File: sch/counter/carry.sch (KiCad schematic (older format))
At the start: 9 parts, among them Q34 Q_NMOS_GSD, Q35 Q_NMOS_GSD

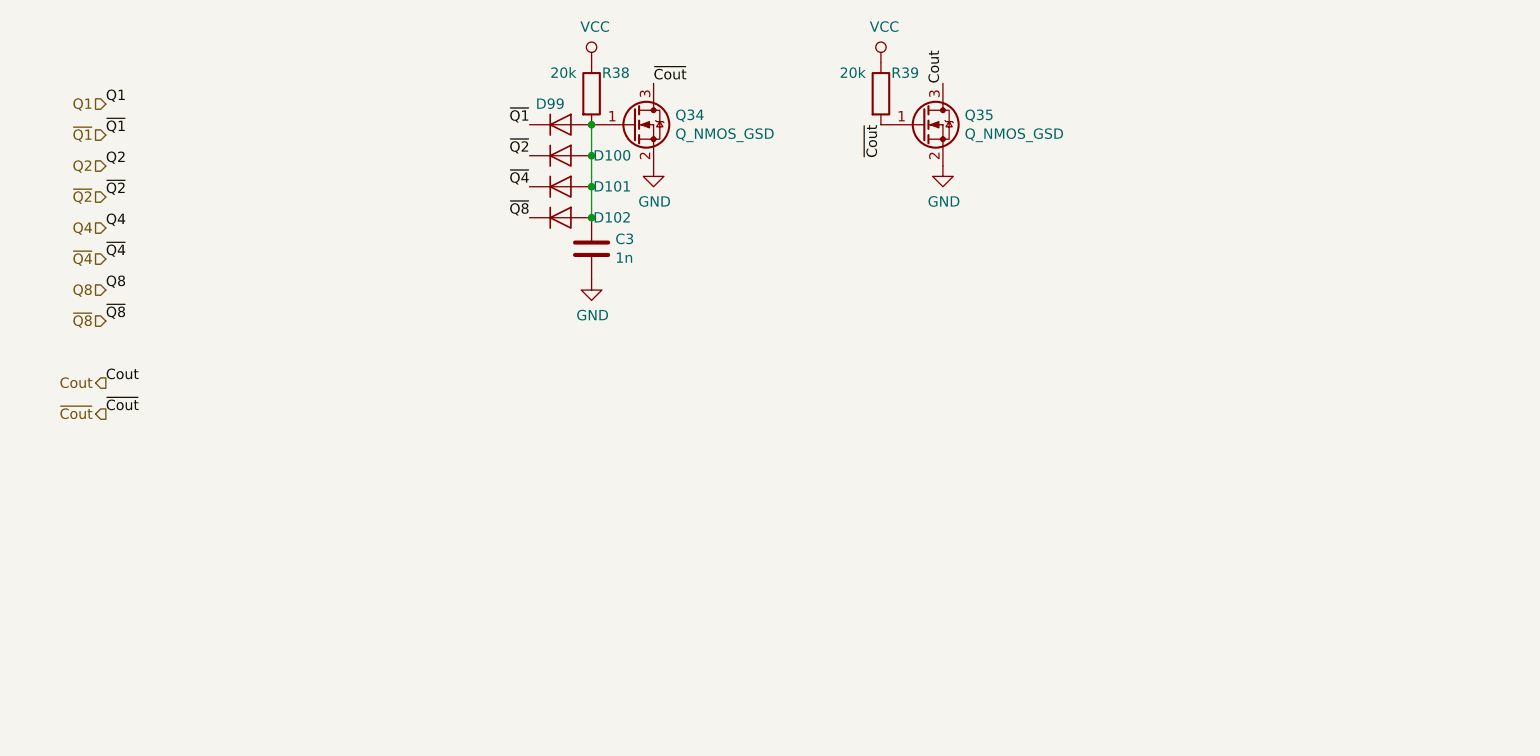
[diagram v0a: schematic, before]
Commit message: Counter schematic improvements
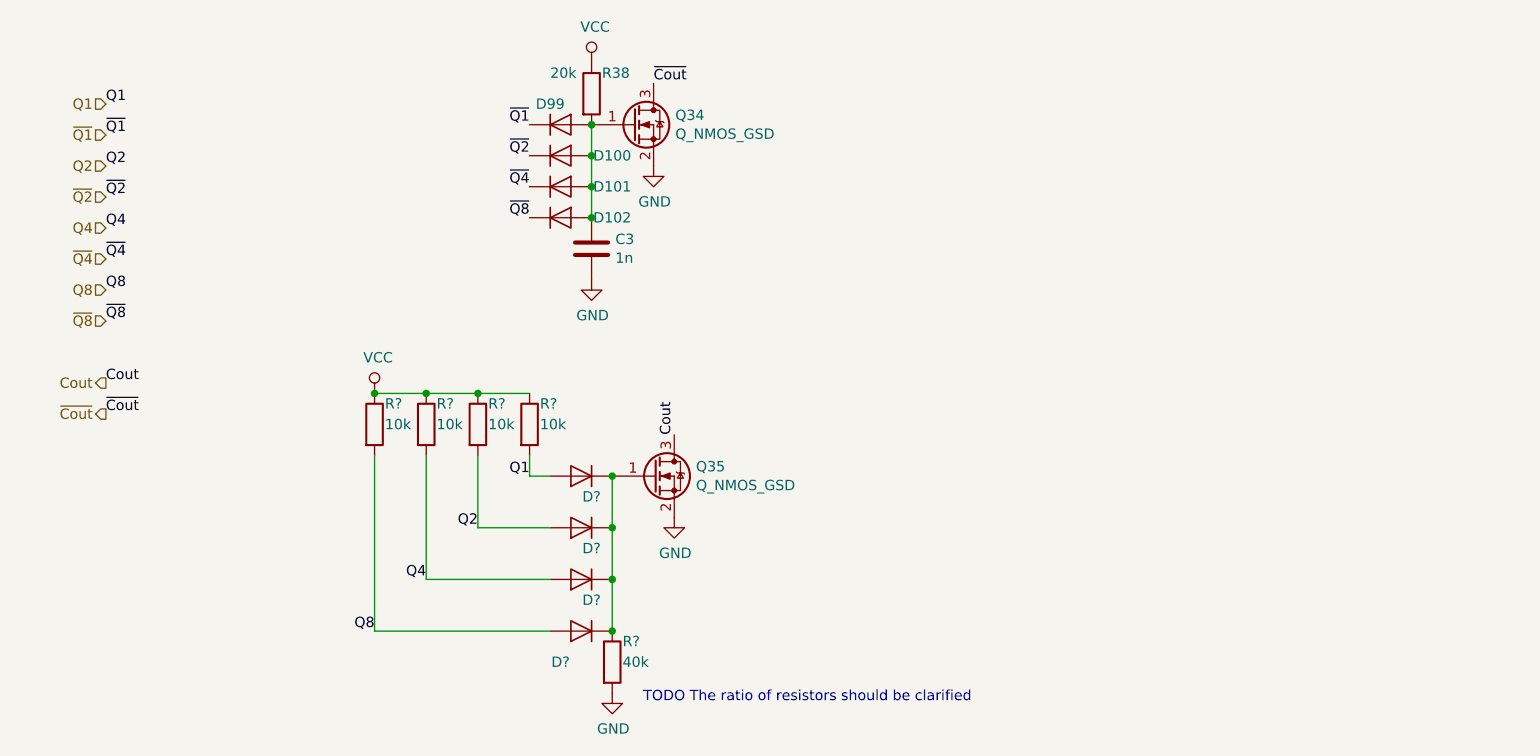
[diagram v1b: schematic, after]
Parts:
- removed R39: 20k, symbol Device:R
- added D? (x4): D, symbol Device:D
- added R? (x4): 10k, symbol Device:R
- added R?: 40k, symbol Device:R
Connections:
- net GND: now also R?.2
- net Q1: now also D?.2 (A), R?.2
- net Q2: now also D?.2 (A), R?.2
- net Q4: now also D?.2 (A), R?.2
- net Q8: now also D?.2 (A), R?.2
- net VCC: now also R?.1, R?.1, R?.1, R?.1
- net ~Cout: no longer Q35.1 (G)
- new net: D?.1 (K), D?.1 (K), D?.1 (K), D?.1 (K), Q35.1 (G), R?.1
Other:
- note added: "TODO The ratio of resistors should be clarified"
- moved on the sheet: Q35

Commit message: One flip-flop is placed on PCB
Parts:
- C3: footprint (none) -> Capacitor_SMD:C_0805_2012Metric
- D100, D101, D102, D99: footprint (none) -> Diode_SMD:D_MiniMELF
- D103, D104, D105, D106: renamed from D?; footprint (none) -> Diode_SMD:D_MiniMELF
- Q34, Q35: footprint (none) -> Package_TO_SOT_SMD:SOT-23
- R38, R39, R40, R41, R43: renamed from R?; footprint (none) -> Resistor_SMD:R_0805_2012Metric
- R42: renamed from R38; footprint (none) -> Resistor_SMD:R_0805_2012Metric
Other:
- note added: "This capacitor is needed to avoid driving ~Cout~ down too quickly.\nThis happens when the lower bits are reset and the higher bit is set (3->4, 1->2, etc.)."
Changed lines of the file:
@@
 EESchema Schematic File Version 4
+LIBS:counter-cache
 EELAYER 26 0
 EELAYER END
@@
 F 0 "Q34" H 4005 1196 50  0000 L CNN
 F 1 "Q_NMOS_GSD" H 4005 1105 50  0000 L CNN
-F 2 "" H 4000 1250 50  0001 C CNN
+F 2 "Package_TO_SOT_SMD:SOT-23" H 4000 1250 50  0001 C CNN
 F 3 "~" H 3800 1150 50  0001 C CNN
 	1    3800 1150
@@
 AR Path="/5BF4F50C/5BF5F56C" Ref="R?"  Part="1"
 AR Path="/5BF4F514/5BF5F56C" Ref="R?"  Part="1"
-AR Path="/5BF5F0A6/5BF5F56C" Ref="R38"  Part="1"
-F 0 "R38" H 3650 1100 50  0000 L CNN
+AR Path="/5BF5F0A6/5BF5F56C" Ref="R42"  Part="1"
+F 0 "R42" H 3650 1100 50  0000 L CNN
 F 1 "20k" H 3400 1100 50  0000 L CNN
-F 2 "" V 3530 1000 50  0001 C CNN
+F 2 "Resistor_SMD:R_0805_2012Metric" V 3530 1000 50  0001 C CNN
 F 3 "~" H 3600 1000 50  0001 C CNN
 	1    3600 1000
@@
 F 0 "D99" H 3400 1250 50  0000 C CNN
 F 1 "D" H 3450 1275 50  0001 C CNN
-F 2 "" H 3450 1150 50  0001 C CNN
+F 2 "Diode_SMD:D_MiniMELF" H 3450 1150 50  0001 C CNN
 F 3 "~" H 3450 1150 50  0001 C CNN
 	1    3450 1150
@@
 F 0 "D100" H 3700 1300 50  0000 C CNN
 F 1 "D" H 3450 1425 50  0001 C CNN
-F 2 "" H 3450 1300 50  0001 C CNN
+F 2 "Diode_SMD:D_MiniMELF" H 3450 1300 50  0001 C CNN
 F 3 "~" H 3450 1300 50  0001 C CNN
 	1    3450 1300
@@
 F 0 "D101" H 3700 1450 50  0000 C CNN
 F 1 "D" H 3200 1450 50  0001 C CNN
-F 2 "" H 3450 1450 50  0001 C CNN
+F 2 "Diode_SMD:D_MiniMELF" H 3450 1450 50  0001 C CNN
 F 3 "~" H 3450 1450 50  0001 C CNN
 	1    3450 1450
@@
 AR Path="/5BF4F50C/5BF5F58F" Ref="#PWR?"  Part="1"
 AR Path="/5BF4F514/5BF5F58F" Ref="#PWR?"  Part="1"
-AR Path="/5BF5F0A6/5BF5F58F" Ref="#PWR077"  Part="1"
-F 0 "#PWR077" H 3600 700 50  0001 C CNN
+AR Path="/5BF5F0A6/5BF5F58F" Ref="#PWR078"  Part="1"
+F 0 "#PWR078" H 3600 700 50  0001 C CNN
 F 1 "VCC" H 3617 1023 50  0000 C CNN
 F 2 "" H 3600 850 50  0001 C CNN
@@
 $EndComp
 $Comp
-L power:GND #PWR079
+L power:GND #PWR081
 U 1 1 5BF5F5F2
 P 3900 1350
-F 0 "#PWR079" H 3900 1100 50  0001 C CNN
+F 0 "#PWR081" H 3900 1100 50  0001 C CNN
 F 1 "GND" H 3905 1177 50  0000 C CNN
 F 2 "" H 3900 1350 50  0001 C CNN
@@
 F 0 "D102" H 3700 1600 50  0000 C CNN
 F 1 "D" H 3450 1725 50  0001 C CNN
-F 2 "" H 3450 1600 50  0001 C CNN
+F 2 "Diode_SMD:D_MiniMELF" H 3450 1600 50  0001 C CNN
 F 3 "~" H 3450 1600 50  0001 C CNN
 	1    3450 1600
@@
 F 0 "C3" H 3715 1796 50  0000 L CNN
 F 1 "1n" H 3715 1705 50  0000 L CNN
-F 2 "" H 3638 1600 50  0001 C CNN
+F 2 "Capacitor_SMD:C_0805_2012Metric" H 3638 1600 50  0001 C CNN
 F 3 "~" H 3600 1750 50  0001 C CNN
 	1    3600 1750
@@
 Connection ~ 3600 1600
 $Comp
-L power:GND #PWR078
+L power:GND #PWR079
 U 1 1 5BF5F81C
 P 3600 1900
-F 0 "#PWR078" H 3600 1650 50  0001 C CNN
+F 0 "#PWR079" H 3600 1650 50  0001 C CNN
 F 1 "GND" H 3605 1727 50  0000 C CNN
 F 2 "" H 3600 1900 50  0001 C CNN
@@
 F 0 "Q35" H 4105 2896 50  0000 L CNN
 F 1 "Q_NMOS_GSD" H 4105 2805 50  0000 L CNN
-F 2 "" H 4100 2950 50  0001 C CNN
+F 2 "Package_TO_SOT_SMD:SOT-23" H 4100 2950 50  0001 C CNN
 F 3 "~" H 3900 2850 50  0001 C CNN
 	1    3900 2850
@@
 $EndComp
 $Comp
-L power:GND #PWR081
+L power:GND #PWR082
 U 1 1 5BF5F8BF
 P 4000 3050
-F 0 "#PWR081" H 4000 2800 50  0001 C CNN
+F 0 "#PWR082" H 4000 2800 50  0001 C CNN
 F 1 "GND" H 4005 2877 50  0000 C CNN
 F 2 "" H 4000 3050 50  0001 C CNN
@@
 AR Path="/5BF4F50C/5BF92A86" Ref="D?"  Part="1"
 AR Path="/5BF4F514/5BF92A86" Ref="D?"  Part="1"
-AR Path="/5BF5F0A6/5BF92A86" Ref="D?"  Part="1"
-F 0 "D?" H 3500 2950 50  0000 C CNN
+AR Path="/5BF5F0A6/5BF92A86" Ref="D103"  Part="1"
+F 0 "D103" H 3500 2950 50  0000 C CNN
 F 1 "D" H 3550 2975 50  0001 C CNN
-F 2 "" H 3550 2850 50  0001 C CNN
+F 2 "Diode_SMD:D_MiniMELF" H 3550 2850 50  0001 C CNN
 F 3 "~" H 3550 2850 50  0001 C CNN
 	1    3550 2850
@@
 AR Path="/5BF4F50C/5BF92B23" Ref="D?"  Part="1"
 AR Path="/5BF4F514/5BF92B23" Ref="D?"  Part="1"
-AR Path="/5BF5F0A6/5BF92B23" Ref="D?"  Part="1"
-F 0 "D?" H 3500 3200 50  0000 C CNN
+AR Path="/5BF5F0A6/5BF92B23" Ref="D104"  Part="1"
+F 0 "D104" H 3500 3200 50  0000 C CNN
 F 1 "D" H 3550 3225 50  0001 C CNN
-F 2 "" H 3550 3100 50  0001 C CNN
+F 2 "Diode_SMD:D_MiniMELF" H 3550 3100 50  0001 C CNN
 F 3 "~" H 3550 3100 50  0001 C CNN
 	1    3550 3100
@@
 AR Path="/5BF4F50C/5BF92B48" Ref="D?"  Part="1"
 AR Path="/5BF4F514/5BF92B48" Ref="D?"  Part="1"
-AR Path="/5BF5F0A6/5BF92B48" Ref="D?"  Part="1"
-F 0 "D?" H 3500 3450 50  0000 C CNN
+AR Path="/5BF5F0A6/5BF92B48" Ref="D105"  Part="1"
+F 0 "D105" H 3500 3450 50  0000 C CNN
 F 1 "D" H 3550 3475 50  0001 C CNN
-F 2 "" H 3550 3350 50  0001 C CNN
+F 2 "Diode_SMD:D_MiniMELF" H 3550 3350 50  0001 C CNN
 F 3 "~" H 3550 3350 50  0001 C CNN
 	1    3550 3350
@@
 AR Path="/5BF4F50C/5BF92B6F" Ref="D?"  Part="1"
 AR Path="/5BF4F514/5BF92B6F" Ref="D?"  Part="1"
-AR Path="/5BF5F0A6/5BF92B6F" Ref="D?"  Part="1"
-F 0 "D?" H 3650 3750 50  0000 C CNN
+AR Path="/5BF5F0A6/5BF92B6F" Ref="D106"  Part="1"
+F 0 "D106" H 3650 3750 50  0000 C CNN
 F 1 "D" H 3550 3725 50  0001 C CNN
-F 2 "" H 3550 3600 50  0001 C CNN
+F 2 "Diode_SMD:D_MiniMELF" H 3550 3600 50  0001 C CNN
 F 3 "~" H 3550 3600 50  0001 C CNN
 	1    3550 3600
@@
 AR Path="/5BF4F50C/5BF92BB5" Ref="R?"  Part="1"
 AR Path="/5BF4F514/5BF92BB5" Ref="R?"  Part="1"
-AR Path="/5BF5F0A6/5BF92BB5" Ref="R?"  Part="1"
-F 0 "R?" H 3350 2700 50  0000 L CNN
+AR Path="/5BF5F0A6/5BF92BB5" Ref="R41"  Part="1"
+F 0 "R41" H 3350 2700 50  0000 L CNN
 F 1 "10k" H 3350 2600 50  0000 L CNN
-F 2 "" V 3230 2600 50  0001 C CNN
+F 2 "Resistor_SMD:R_0805_2012Metric" V 3230 2600 50  0001 C CNN
 F 3 "~" H 3300 2600 50  0001 C CNN
 	1    3300 2600
@@
 AR Path="/5BF4F50C/5BF92C6F" Ref="R?"  Part="1"
 AR Path="/5BF4F514/5BF92C6F" Ref="R?"  Part="1"
-AR Path="/5BF5F0A6/5BF92C6F" Ref="R?"  Part="1"
-F 0 "R?" H 3100 2700 50  0000 L CNN
+AR Path="/5BF5F0A6/5BF92C6F" Ref="R40"  Part="1"
+F 0 "R40" H 3100 2700 50  0000 L CNN
 F 1 "10k" H 3100 2600 50  0000 L CNN
-F 2 "" V 2980 2600 50  0001 C CNN
+F 2 "Resistor_SMD:R_0805_2012Metric" V 2980 2600 50  0001 C CNN
 F 3 "~" H 3050 2600 50  0001 C CNN
 	1    3050 2600
@@
 AR Path="/5BF4F50C/5BF92CA0" Ref="R?"  Part="1"
 AR Path="/5BF4F514/5BF92CA0" Ref="R?"  Part="1"
-AR Path="/5BF5F0A6/5BF92CA0" Ref="R?"  Part="1"
-F 0 "R?" H 2850 2700 50  0000 L CNN
+AR Path="/5BF5F0A6/5BF92CA0" Ref="R39"  Part="1"
+F 0 "R39" H 2850 2700 50  0000 L CNN
 F 1 "10k" H 2850 2600 50  0000 L CNN
-F 2 "" V 2730 2600 50  0001 C CNN
+F 2 "Resistor_SMD:R_0805_2012Metric" V 2730 2600 50  0001 C CNN
 F 3 "~" H 2800 2600 50  0001 C CNN
 	1    2800 2600
@@
 AR Path="/5BF4F50C/5BF92CD1" Ref="R?"  Part="1"
 AR Path="/5BF4F514/5BF92CD1" Ref="R?"  Part="1"
-AR Path="/5BF5F0A6/5BF92CD1" Ref="R?"  Part="1"
-F 0 "R?" H 2600 2700 50  0000 L CNN
+AR Path="/5BF5F0A6/5BF92CD1" Ref="R38"  Part="1"
+F 0 "R38" H 2600 2700 50  0000 L CNN
 F 1 "10k" H 2600 2600 50  0000 L CNN
-F 2 "" V 2480 2600 50  0001 C CNN
+F 2 "Resistor_SMD:R_0805_2012Metric" V 2480 2600 50  0001 C CNN
 F 3 "~" H 2550 2600 50  0001 C CNN
 	1    2550 2600
@@
 AR Path="/5BF4F50C/5BF93187" Ref="#PWR?"  Part="1"
 AR Path="/5BF4F514/5BF93187" Ref="#PWR?"  Part="1"
-AR Path="/5BF5F0A6/5BF93187" Ref="#PWR?"  Part="1"
-F 0 "#PWR?" H 2550 2300 50  0001 C CNN
+AR Path="/5BF5F0A6/5BF93187" Ref="#PWR077"  Part="1"
+F 0 "#PWR077" H 2550 2300 50  0001 C CNN
 F 1 "VCC" H 2567 2623 50  0000 C CNN
 F 2 "" H 2550 2450 50  0001 C CNN
@@
 AR Path="/5BF4F50C/5BF931B2" Ref="R?"  Part="1"
 AR Path="/5BF4F514/5BF931B2" Ref="R?"  Part="1"
-AR Path="/5BF5F0A6/5BF931B2" Ref="R?"  Part="1"
-F 0 "R?" H 3750 3850 50  0000 L CNN
+AR Path="/5BF5F0A6/5BF931B2" Ref="R43"  Part="1"
+F 0 "R43" H 3750 3850 50  0000 L CNN
 F 1 "40k" H 3750 3750 50  0000 L CNN
-F 2 "" V 3630 3750 50  0001 C CNN
+F 2 "Resistor_SMD:R_0805_2012Metric" V 3630 3750 50  0001 C CNN
 F 3 "~" H 3700 3750 50  0001 C CNN
 	1    3700 3750
@@
 Connection ~ 3700 3600
 $Comp
-L power:GND #PWR?
+L power:GND #PWR080
 U 1 1 5BF9328A
 P 3700 3900
-F 0 "#PWR?" H 3700 3650 50  0001 C CNN
+F 0 "#PWR080" H 3700 3650 50  0001 C CNN
 F 1 "GND" H 3705 3727 50  0000 C CNN
 F 2 "" H 3700 3900 50  0001 C CNN
@@
 Text Notes 3850 3950 0    50   ~ 0
 TODO The ratio of resistors should be clarified
+Text Notes 3900 1850 0    50   ~ 0
+This capacitor is needed to avoid driving ~Cout~ down too quickly.\nThis happens when the lower bits are reset and the higher bit is set (3->4, 1->2, etc.).
 $EndSCHEMATC

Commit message: Added datasheets, set component values, calculated LED resistors
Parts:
- D100, D101, D102, D103, D104, D105, D106, D99: value D -> LL103C
- Q34, Q35: value Q_NMOS_GSD -> 2N7002
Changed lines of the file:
@@
 AR Path="/5BF5F0A6/5BF5F565" Ref="Q34"  Part="1"
 F 0 "Q34" H 4005 1196 50  0000 L CNN
-F 1 "Q_NMOS_GSD" H 4005 1105 50  0000 L CNN
+F 1 "2N7002" H 4005 1105 50  0000 L CNN
 F 2 "Package_TO_SOT_SMD:SOT-23" H 4000 1250 50  0001 C CNN
 F 3 "~" H 3800 1150 50  0001 C CNN
@@
 AR Path="/5BF5F0A6/5BF5F573" Ref="D99"  Part="1"
 F 0 "D99" H 3400 1250 50  0000 C CNN
-F 1 "D" H 3450 1275 50  0001 C CNN
+F 1 "LL103C" H 3450 1275 50  0001 C CNN
 F 2 "Diode_SMD:D_MiniMELF" H 3450 1150 50  0001 C CNN
 F 3 "~" H 3450 1150 50  0001 C CNN
@@
 AR Path="/5BF5F0A6/5BF5F57B" Ref="D100"  Part="1"
 F 0 "D100" H 3700 1300 50  0000 C CNN
-F 1 "D" H 3450 1425 50  0001 C CNN
+F 1 "LL103C" H 3450 1425 50  0001 C CNN
 F 2 "Diode_SMD:D_MiniMELF" H 3450 1300 50  0001 C CNN
 F 3 "~" H 3450 1300 50  0001 C CNN
@@
 AR Path="/5BF5F0A6/5BF5F582" Ref="D101"  Part="1"
 F 0 "D101" H 3700 1450 50  0000 C CNN
-F 1 "D" H 3200 1450 50  0001 C CNN
+F 1 "LL103C" H 3200 1450 50  0001 C CNN
 F 2 "Diode_SMD:D_MiniMELF" H 3450 1450 50  0001 C CNN
 F 3 "~" H 3450 1450 50  0001 C CNN
@@
 AR Path="/5BF5F0A6/5BF5F60E" Ref="D102"  Part="1"
 F 0 "D102" H 3700 1600 50  0000 C CNN
-F 1 "D" H 3450 1725 50  0001 C CNN
+F 1 "LL103C" H 3450 1725 50  0001 C CNN
 F 2 "Diode_SMD:D_MiniMELF" H 3450 1600 50  0001 C CNN
 F 3 "~" H 3450 1600 50  0001 C CNN
@@
 AR Path="/5BF5F0A6/5BF5F885" Ref="Q35"  Part="1"
 F 0 "Q35" H 4105 2896 50  0000 L CNN
-F 1 "Q_NMOS_GSD" H 4105 2805 50  0000 L CNN
+F 1 "2N7002" H 4105 2805 50  0000 L CNN
 F 2 "Package_TO_SOT_SMD:SOT-23" H 4100 2950 50  0001 C CNN
 F 3 "~" H 3900 2850 50  0001 C CNN
@@
 AR Path="/5BF5F0A6/5BF92A86" Ref="D103"  Part="1"
 F 0 "D103" H 3500 2950 50  0000 C CNN
-F 1 "D" H 3550 2975 50  0001 C CNN
+F 1 "LL103C" H 3550 2975 50  0001 C CNN
 F 2 "Diode_SMD:D_MiniMELF" H 3550 2850 50  0001 C CNN
 F 3 "~" H 3550 2850 50  0001 C CNN
@@
 AR Path="/5BF5F0A6/5BF92B23" Ref="D104"  Part="1"
 F 0 "D104" H 3500 3200 50  0000 C CNN
-F 1 "D" H 3550 3225 50  0001 C CNN
+F 1 "LL103C" H 3550 3225 50  0001 C CNN
 F 2 "Diode_SMD:D_MiniMELF" H 3550 3100 50  0001 C CNN
 F 3 "~" H 3550 3100 50  0001 C CNN
@@
 AR Path="/5BF5F0A6/5BF92B48" Ref="D105"  Part="1"
 F 0 "D105" H 3500 3450 50  0000 C CNN
-F 1 "D" H 3550 3475 50  0001 C CNN
+F 1 "LL103C" H 3550 3475 50  0001 C CNN
 F 2 "Diode_SMD:D_MiniMELF" H 3550 3350 50  0001 C CNN
 F 3 "~" H 3550 3350 50  0001 C CNN
@@
 AR Path="/5BF5F0A6/5BF92B6F" Ref="D106"  Part="1"
 F 0 "D106" H 3650 3750 50  0000 C CNN
-F 1 "D" H 3550 3725 50  0001 C CNN
+F 1 "LL103C" H 3550 3725 50  0001 C CNN
 F 2 "Diode_SMD:D_MiniMELF" H 3550 3600 50  0001 C CNN
 F 3 "~" H 3550 3600 50  0001 C CNN
